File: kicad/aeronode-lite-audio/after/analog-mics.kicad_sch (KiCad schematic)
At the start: 15 parts, among them J20 BOOM VOICE MIC, J21 ANC FEEDFORWARD, J22 ANC FEEDBACK

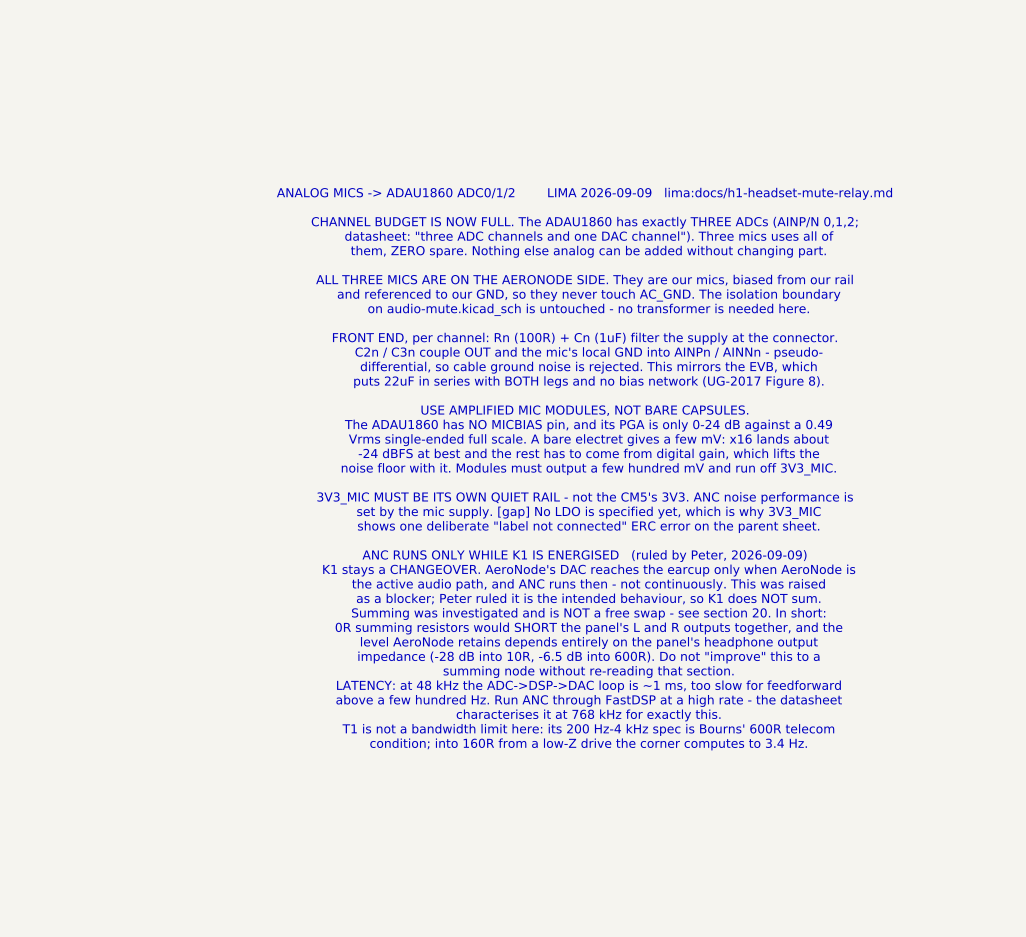
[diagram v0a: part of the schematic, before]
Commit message: [LIMA] audio-mute: K1 sums after all - ANC always on, and 0R would have shorted the panel
Peter retracted the cancel, so section 20 is withdrawn and the summing change is
made. I asked which statement was being withdrawn rather than guessing - the two
readings gave opposite circuits, and picking wrong would have written a false
ruling into the record as well as the wrong copper.

  R1/R2: K1.14/24 -> HS_L/HS_R, permanent. K1's NO contacts unused.
  K1 now breaks only the intercom. MUTE_L/MUTE_R nets gone.
  K1 de-energised: HS_L/HS_R <- AC_L/AC_R + AeroNode, summed.
  K1 energised:    intercom OPEN, AeroNode alone.

R1/R2 changed 0R -> 220R, and had to. AERONODE_AUDIO ties the two channels, so
0R would SHORT the panel's left and right outputs together. That was harmless
under the changeover because the intercom was open at the same instant; summing
keeps it connected. The value had to change because the switch behaviour around
it changed, not because the part did. 220R gives a 440R L-to-R path for only
1.4 dB less level than 100R.

Netlist verified: HS_L -> J11.1, K1.11, R1.1; AERONODE_AUDIO -> R1.2, R2.2,
R4.1, T1.4. ERC 42 = 41 baseline + the deliberate 3V3_MIC error.

Honest limit recorded: the DAC now always reaches the earcup, but a passive sum
cannot fight a low-Z source. Intercom live, AeroNode sits ~-33 dB; when K1 opens
the intercom it jumps to -7.6 dB. So ANC AUTHORITY in normal flight is set by
the panel's headphone output impedance, which is unmeasured. Stiff panel and ANC
will not do useful work summed - it would need its own path to the transducer.

Co-Authored-By: Claude Opus 5 <noreply@anthropic.com>
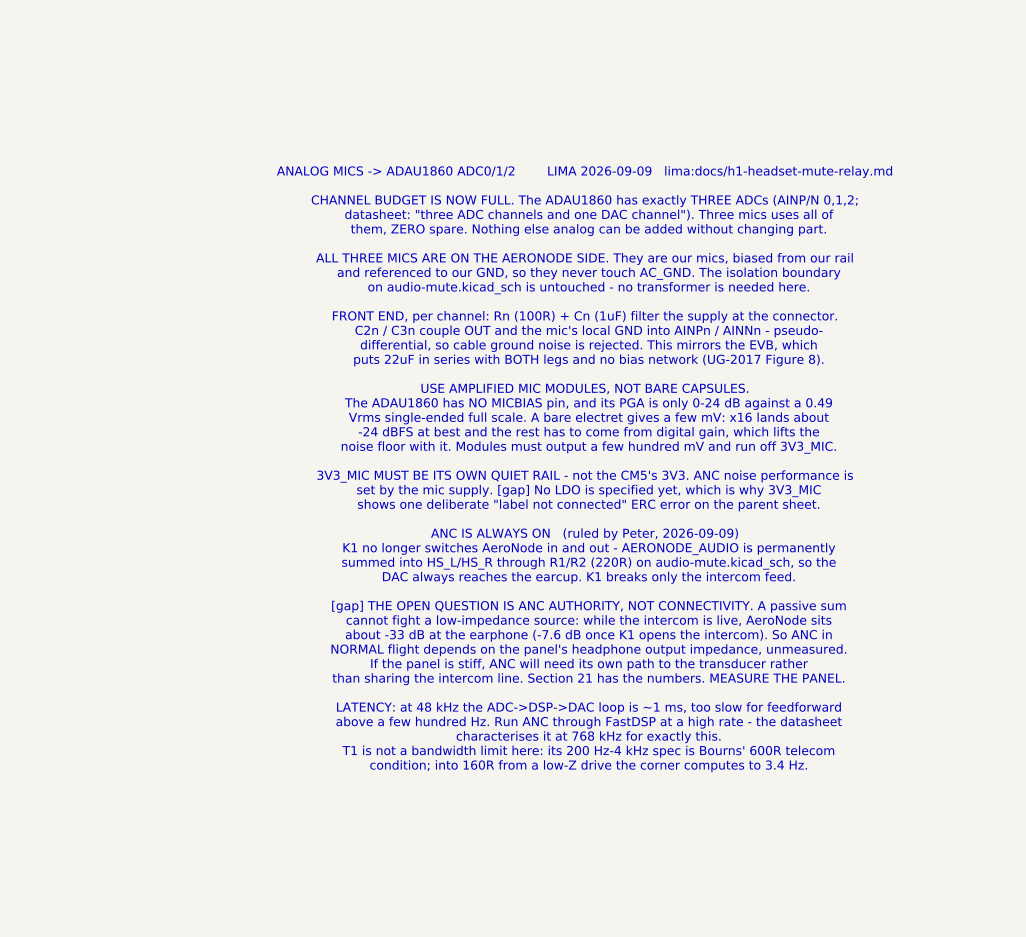
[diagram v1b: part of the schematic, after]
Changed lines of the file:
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@@
 		)
 	)
-  (text "ANALOG MICS -> ADAU1860 ADC0/1/2        LIMA 2026-09-09   lima:docs/h1-headset-mute-relay.md\n\nCHANNEL BUDGET IS NOW FULL. The ADAU1860 has exactly THREE ADCs (AINP/N 0,1,2;\n  datasheet: \"three ADC channels and one DAC channel\"). Three mics uses all of\n  them, ZERO spare. Nothing else analog can be added without changing part.\n\nALL THREE MICS ARE ON THE AERONODE SIDE. They are our mics, biased from our rail\n  and referenced to our GND, so they never touch AC_GND. The isolation boundary\n  on audio-mute.kicad_sch is untouched - no transformer is needed here.\n\nFRONT END, per channel: Rn (100R) + Cn (1uF) filter the supply at the connector.\n  C2n / C3n couple OUT and the mic's local GND into AINPn / AINNn - pseudo-\n  differential, so cable ground noise is rejected. This mirrors the EVB, which\n  puts 22uF in series with BOTH legs and no bias network (UG-2017 Figure 8).\n\nUSE AMPLIFIED MIC MODULES, NOT BARE CAPSULES.\n  The ADAU1860 has NO MICBIAS pin, and its PGA is only 0-24 dB against a 0.49\n  Vrms single-ended full scale. A bare electret gives a few mV: x16 lands about\n  -24 dBFS at best and the rest has to come from digital gain, which lifts the\n  noise floor with it. Modules must output a few hundred mV and run off 3V3_MIC.\n\n3V3_MIC MUST BE ITS OWN QUIET RAIL - not the CM5's 3V3. ANC noise performance is\n  set by the mic supply. [gap] No LDO is specified yet, which is why 3V3_MIC\n  shows one deliberate \"label not connected\" ERC error on the parent sheet.\n\nANC RUNS ONLY WHILE K1 IS ENERGISED   (ruled by Peter, 2026-09-09)\n  K1 stays a CHANGEOVER. AeroNode's DAC reaches the earcup only when AeroNode is\n  the active audio path, and ANC runs then - not continuously. This was raised\n  as a blocker; Peter ruled it is the intended behaviour, so K1 does NOT sum.\n  Summing was investigated and is NOT a free swap - see section 20. In short:\n  0R summing resistors would SHORT the panel's L and R outputs together, and the\n  level AeroNode retains depends entirely on the panel's headphone output\n  impedance (-28 dB into 10R, -6.5 dB into 600R). Do not \"improve\" this to a\n  summing node without re-reading that section.\n  LATENCY: at 48 kHz the ADC->DSP->DAC loop is ~1 ms, too slow for feedforward\n  above a few hundred Hz. Run ANC through FastDSP at a high rate - the datasheet\n  characterises it at 768 kHz for exactly this.\n  T1 is not a bandwidth limit here: its 200 Hz-4 kHz spec is Bourns' 600R telecom\n  condition; into 160R from a low-Z drive the corner computes to 3.4 Hz."
+  (text "ANALOG MICS -> ADAU1860 ADC0/1/2        LIMA 2026-09-09   lima:docs/h1-headset-mute-relay.md\n\nCHANNEL BUDGET IS NOW FULL. The ADAU1860 has exactly THREE ADCs (AINP/N 0,1,2;\n  datasheet: \"three ADC channels and one DAC channel\"). Three mics uses all of\n  them, ZERO spare. Nothing else analog can be added without changing part.\n\nALL THREE MICS ARE ON THE AERONODE SIDE. They are our mics, biased from our rail\n  and referenced to our GND, so they never touch AC_GND. The isolation boundary\n  on audio-mute.kicad_sch is untouched - no transformer is needed here.\n\nFRONT END, per channel: Rn (100R) + Cn (1uF) filter the supply at the connector.\n  C2n / C3n couple OUT and the mic's local GND into AINPn / AINNn - pseudo-\n  differential, so cable ground noise is rejected. This mirrors the EVB, which\n  puts 22uF in series with BOTH legs and no bias network (UG-2017 Figure 8).\n\nUSE AMPLIFIED MIC MODULES, NOT BARE CAPSULES.\n  The ADAU1860 has NO MICBIAS pin, and its PGA is only 0-24 dB against a 0.49\n  Vrms single-ended full scale. A bare electret gives a few mV: x16 lands about\n  -24 dBFS at best and the rest has to come from digital gain, which lifts the\n  noise floor with it. Modules must output a few hundred mV and run off 3V3_MIC.\n\n3V3_MIC MUST BE ITS OWN QUIET RAIL - not the CM5's 3V3. ANC noise performance is\n  set by the mic supply. [gap] No LDO is specified yet, which is why 3V3_MIC\n  shows one deliberate \"label not connected\" ERC error on the parent sheet.\n\nANC IS ALWAYS ON   (ruled by Peter, 2026-09-09)\n  K1 no longer switches AeroNode in and out - AERONODE_AUDIO is permanently\n  summed into HS_L/HS_R through R1/R2 (220R) on audio-mute.kicad_sch, so the\n  DAC always reaches the earcup. K1 breaks only the intercom feed.\n\n  [gap] THE OPEN QUESTION IS ANC AUTHORITY, NOT CONNECTIVITY. A passive sum\n  cannot fight a low-impedance source: while the intercom is live, AeroNode sits\n  about -33 dB at the earphone (-7.6 dB once K1 opens the intercom). So ANC in\n  NORMAL flight depends on the panel's headphone output impedance, unmeasured.\n  If the panel is stiff, ANC will need its own path to the transducer rather\n  than sharing the intercom line. Section 21 has the numbers. MEASURE THE PANEL.\n\n  LATENCY: at 48 kHz the ADC->DSP->DAC loop is ~1 ms, too slow for feedforward\n  above a few hundred Hz. Run ANC through FastDSP at a high rate - the datasheet\n  characterises it at 768 kHz for exactly this.\n  T1 is not a bandwidth limit here: its 200 Hz-4 kHz spec is Bourns' 600R telecom\n  condition; into 160R from a low-Z drive the corner computes to 3.4 Hz."
     (at 195 85 0)
     (effects (font (size 1 1)))
